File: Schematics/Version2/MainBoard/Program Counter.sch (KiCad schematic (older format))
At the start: 9 parts, among them J3 Program Counter LED Connector, U18 74F161, U19 74F161, U20 74F161, U21 74F161

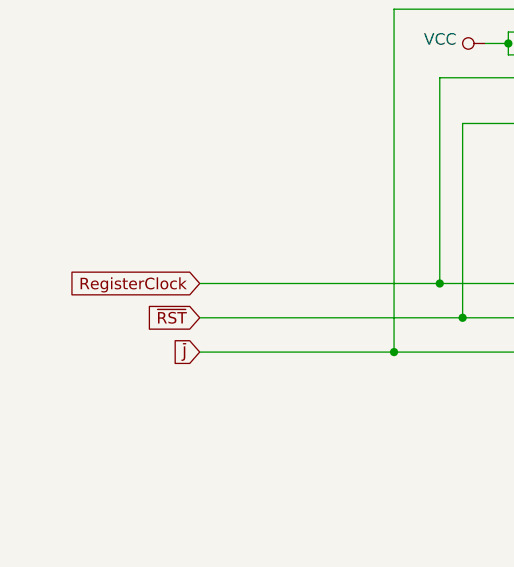
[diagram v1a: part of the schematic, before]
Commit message: Merge branch "version2b".
This is a new version of the computer which incorporates a number of
improvements:
  * Uses a four layer PCB instead of six.
  * Replaced the clock with a new circuit. This is simpler, but allows for
    an external clock to be attached.
  * Changes to the ALU to have it operate over two clock cycles instead of
    one. This fixes a timing issue which makes the ALU unreliable at 10MHz.
  * Replaced instruction RAM with dual port SRAM.
  * Replaced the physical connector for expansion cards to interleave
    signals with ground.
  * Added places where components can be attached to provide AC termination
    of the data bus, should this be necessary.
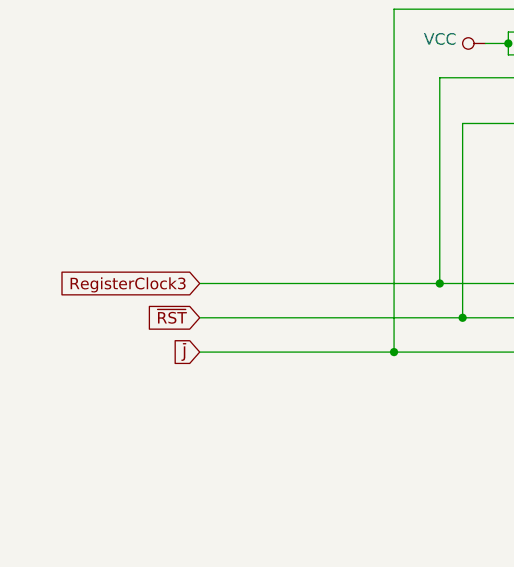
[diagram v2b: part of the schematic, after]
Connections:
- net RegisterClock renamed RegisterClock3
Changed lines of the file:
@@
 $Descr USLetter 11000 8500
 encoding utf-8
-Sheet 4 23
+Sheet 3 21
 Title "Program Counter"
 Date ""
@@
 	2200 3950 1050 3950
 Text GLabel 1050 3800 0    50   Input ~ 0
-RegisterClock
+RegisterClock3
 Wire Wire Line
 	2500 2900 2100 2900
